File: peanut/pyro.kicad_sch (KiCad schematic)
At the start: 20 parts, among them J1 PYRO_1, J2 PYRO_1, Q1 NMOS, Q2 NMOS, Q3 NMOS, Q4 NMOS

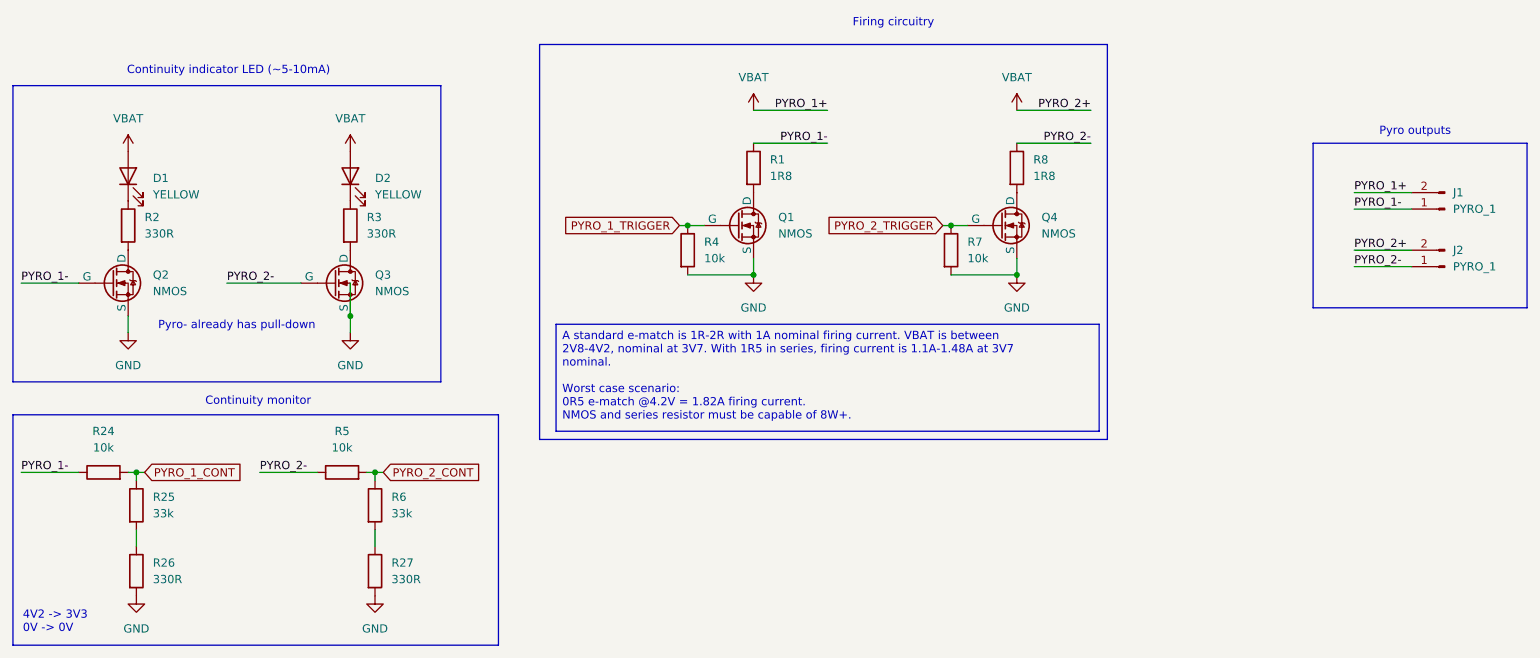
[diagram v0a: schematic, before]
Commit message: Assigned some actual parts and footprints to symbols.
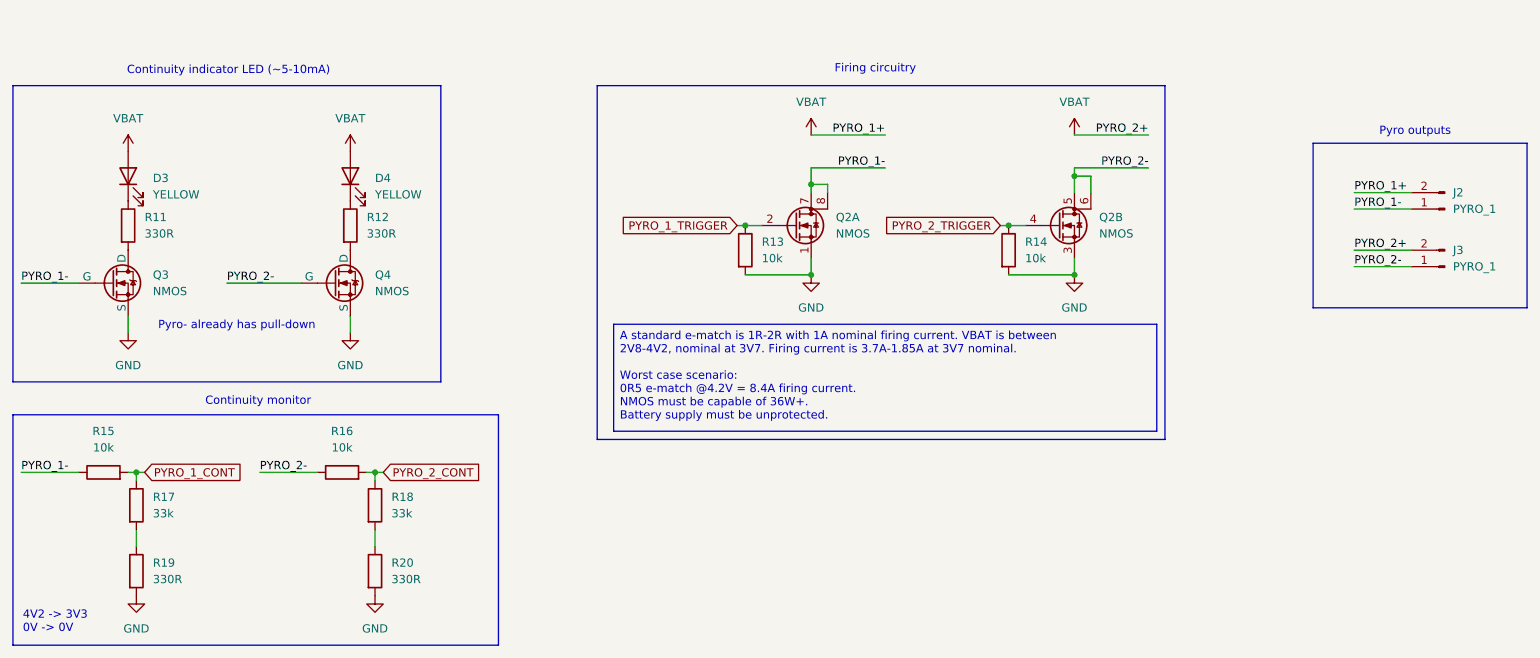
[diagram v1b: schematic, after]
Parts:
- removed Q1, Q4: NMOS, symbol Simulation_SPICE:NMOS
- removed R1, R8: 1R8, symbol Device:R
- added Q2: NMOS, symbol Transistor_FET:Q_Dual_NMOS_S1G1S2G2D2D2D1D1
- D3: renamed from D1; footprint (none) -> LED_SMD:LED_0402_1005Metric
- D4: renamed from D2; footprint (none) -> LED_SMD:LED_0402_1005Metric
- J3: renamed from J2; footprint (none) -> Connector_USB:USB_C_Receptacle_GCT_USB4105-xx-A_16P_TopMnt_Horizontal
- R11: renamed from R2; footprint (none) -> Resistor_SMD:R_0402_1005Metric
- R12: renamed from R3; footprint (none) -> Resistor_SMD:R_0402_1005Metric
- R13: renamed from R4; footprint (none) -> Resistor_SMD:R_0402_1005Metric
- R14: renamed from R7; footprint (none) -> Resistor_SMD:R_0402_1005Metric
- R15: renamed from R24; footprint (none) -> Resistor_SMD:R_0402_1005Metric
- R16: renamed from R5; footprint (none) -> Resistor_SMD:R_0402_1005Metric
- R17: renamed from R25; footprint (none) -> Resistor_SMD:R_0402_1005Metric
- R18: renamed from R6; footprint (none) -> Resistor_SMD:R_0402_1005Metric
- R19: renamed from R26; footprint (none) -> Resistor_SMD:R_0402_1005Metric
- R20: renamed from R27; footprint (none) -> Resistor_SMD:R_0402_1005Metric
- renumbered J1 to J2, Q2 to Q3, Q3 to Q4
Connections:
- net GND: now also Q2.1 (S), Q2.3 (S)
- net PYRO_1-: now also Q2.7 (D), Q2.8 (D)
- net PYRO_1_TRIGGER: now also Q2.2 (G)
- net PYRO_2-: now also Q2.5 (D), Q2.6 (D)
- net PYRO_2_TRIGGER: now also Q2.4 (G)
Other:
- moved on the sheet: R13, R14

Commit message: Footprint assignments for dual-channel NMOS; picked some more parts
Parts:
- D3, D4: MPN (none) -> 599-1140-147F
- Q2: footprint (none) -> TSM200N03DPQ33_RGG:TSM200N03DPQ33RGG
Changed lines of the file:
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@@
 			)
 		)
-		(property "Footprint" ""
+		(property "Footprint" "TSM200N03DPQ33_RGG:TSM200N03DPQ33RGG"
 			(at 199.39 104.14 0)
 			(effects
@@
 			)
 		)
-		(property "Datasheet" "https://www.taiwansemi.com/assets/datasheet/pdf.php?pn=TSM200N03DPQ33"
+		(property "Datasheet" "~"
 			(at 199.39 104.14 0)
 			(effects
@@
 			)
 		)
-		(property "MPN" ""
+		(property "MPN" " 599-1140-147F"
 			(at 85.09 96.52 90)
 			(effects
@@
 			)
 		)
-		(property "MPN" ""
+		(property "MPN" " 599-1140-147F"
 			(at 50.8 96.52 90)
 			(effects
@@
 			)
 		)
-		(property "Footprint" ""
+		(property "Footprint" "TSM200N03DPQ33_RGG:TSM200N03DPQ33RGG"
 			(at 158.75 104.14 0)
 			(effects

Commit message: More component MPNs
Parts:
- D3, D4: MPN 599-1140-147F -> 599-1140-147F
- J3: footprint Connector_USB:USB_C_Receptacle_GCT_USB4105-xx-A_16P_TopMnt_Horizontal -> (none)
- R11, R12, R19, R20: MPN (none) -> 560112110231
- R13, R14, R15, R16: MPN (none) -> SFR01MZPJ103
- R17, R18: MPN (none) -> MR04X3302FTL
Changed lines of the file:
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@@
 			)
 		)
-		(property "MPN" ""
+		(property "MPN" "SFR01MZPJ103"
 			(at 186.69 107.95 0)
 			(effects
@@
 			)
 		)
-		(property "Footprint" "Connector_USB:USB_C_Receptacle_GCT_USB4105-xx-A_16P_TopMnt_Horizontal"
+		(property "Footprint" ""
 			(at 254 110.49 0)
 			(effects
@@
 			)
 		)
-		(property "MPN" ""
+		(property "MPN" "MR04X3302FTL"
 			(at 88.9 147.32 0)
 			(effects
@@
 			)
 		)
-		(property "MPN" " 599-1140-147F"
+		(property "MPN" "599-1140-147F"
 			(at 85.09 96.52 90)
 			(effects
@@
 			)
 		)
-		(property "MPN" ""
+		(property "MPN" "560112110231"
 			(at 85.09 104.14 0)
 			(effects
@@
 			)
 		)
-		(property "MPN" ""
+		(property "MPN" "560112110231"
 			(at 88.9 157.48 0)
 			(effects
@@
 			)
 		)
-		(property "MPN" ""
+		(property "MPN" "560112110231"
 			(at 52.07 157.48 0)
 			(effects
@@
 			)
 		)
-		(property "MPN" " 599-1140-147F"
+		(property "MPN" "599-1140-147F"
 			(at 50.8 96.52 90)
 			(effects
@@
 			)
 		)
-		(property "MPN" ""
+		(property "MPN" "SFR01MZPJ103"
 			(at 83.82 142.24 90)
 			(effects
@@
 			)
 		)
-		(property "MPN" ""
+		(property "MPN" "SFR01MZPJ103"
 			(at 146.05 107.95 0)
 			(effects
@@
 			)
 		)
-		(property "MPN" ""
+		(property "MPN" "SFR01MZPJ103"
 			(at 46.99 142.24 90)
 			(effects
@@
 			)
 		)
-		(property "MPN" ""
+		(property "MPN" "MR04X3302FTL"
 			(at 52.07 147.32 0)
 			(effects
@@
 			)
 		)
-		(property "MPN" ""
+		(property "MPN" "560112110231"
 			(at 50.8 104.14 0)
 			(effects

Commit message: feat: Finish schematic
This commit "completes" the schematic to the best of my foresight for
the moment. All components have BOM MPNs and footprints assigned. I have
double checked pins on the 40MHz clock and that pin assignments on the
MCU are valid. I have selected a chip antenna with high gain, added
decoupling capacitors to the MCU, picked out terminal blocks and
followed the Espressif schematic guide. A preliminary layout can be
made.
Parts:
- removed J2, J3: PYRO_1, symbol Connector:Conn_01x02_Pin
- added J2: PYRO_OUT, TerminalBlock_Phoenix:TerminalBlock_Phoenix_MKDS-1-4-3.81_1x04_P3.81mm_Horizontal, symbol Connector_Generic:Conn_01x04
- Q2: renamed from Q3; footprint (none) -> Package_TO_SOT_SMD:SOT-23-3; MPN (none) -> BSS123NH6327XTSA1
- Q3: renamed from Q4; footprint (none) -> Package_TO_SOT_SMD:SOT-23-3; MPN (none) -> BSS123NH6327XTSA1
- renumbered Q2 to Q4, R15 to R11, R11 to R12, R17 to R13, R19 to R14, R16 to R15, R12 to R16, R18 to R17, R20 to R18, R13 to R19, R14 to R20
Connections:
- net PYRO_1-: now also J2.2 (Pin_2)
- net PYRO_2-: now also J2.4 (Pin_4)
- net VBAT: now also J2.1 (Pin_1), J2.3 (Pin_3)

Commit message: feat: Initial layout
I have roughed out the initial PCB layout. It is wider than I'd like,
and not near a peanut shape. It appears the "start" and "panic" LEDs
never had pins assigned to them. I think I will replace the MCU RX & TX
with these instead, since I can still use the RX and TX as probe pads
that way.
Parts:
- D3, D4: footprint LED_SMD:LED_0402_1005Metric -> LED_SMD:LED_0805_2012Metric
- Q2, Q3: symbol Simulation_SPICE:NMOS -> Transistor_FET_Other:Q_NMOS_Depletion_GSD
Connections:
- net GND: now also Q2.2 (S), Q3.2 (S); no longer Q2.3 (S), Q3.3 (S)
- net PYRO_1-: now also J2.4 (Pin_4), Q2.1 (G); no longer J2.2 (Pin_2), Q2.2 (G)
- net PYRO_2-: now also J2.2 (Pin_2), Q3.1 (G); no longer J2.4 (Pin_4), Q3.2 (G)
- net at R16.2: now also Q3.3 (D); no longer Q3.1 (D)
- net at R12.2: now also Q2.3 (D); no longer Q2.1 (D)
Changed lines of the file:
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@@
 	)
 	(label "PYRO_2-"
-		(at 237.49 104.14 0)
+		(at 237.49 99.06 0)
 		(effects
 			(font
@@
 		)
 	)
-	(label "PYRO_2+"
-		(at 237.49 101.6 0)
-		(effects
-			(font
-				(size 1.27 1.27)
-			)
-			(justify left bottom)
-		)
-	)
-	(label "PYRO_1+"
-		(at 237.49 96.52 0)
+	(label "PYRO_1-"
+		(at 237.49 104.14 0)
 		(effects
 			(font
@@
 		)
 	)
+	(label "PYRO_1+"
+		(at 237.49 101.6 0)
+		(effects
+			(font
+				(size 1.27 1.27)
+			)
+			(justify left bottom)
+		)
+	)
 	(label "PYRO_1-"
 		(at 34.29 142.24 0)
@@
 		)
 	)
-	(label "PYRO_1-"
-		(at 237.49 99.06 0)
+	(label "PYRO_2+"
+		(at 237.49 96.52 0)
 		(effects
 			(font
@@
 			)
 		)
-		(property "Footprint" "LED_SMD:LED_0402_1005Metric"
+		(property "Footprint" "LED_SMD:LED_0805_2012Metric"
 			(at 85.09 96.52 0)
 			(hide yes)
@@
 	)
 	(symbol
-		(lib_id "Simulation_SPICE:NMOS")
+		(lib_id "Transistor_FET_Other:Q_NMOS_Depletion_GSD")
 		(at 48.26 113.03 0)
 		(unit 1)
@@
 		)
 		(property "Footprint" "Package_TO_SOT_SMD:SOT-23-3"
-			(at 53.34 110.49 0)
+			(at 48.26 113.03 0)
 			(hide yes)
 			(show_name no)
@@
 		)
 		(property "Datasheet" "https://www.mouser.ca/datasheet/3/70/1/Infineon_BSS123N_DataSheet_v02_03_en.pdf"
-			(at 48.26 125.73 0)
-			(hide yes)
-			(show_name no)
-			(do_not_autoplace no)
-			(effects
-				(font
-					(size 1.27 1.27)
-				)
-			)
-		)
-		(property "Description" "N-MOSFET transistor, drain/source/gate"
+			(at 48.26 113.03 0)
+			(hide yes)
+			(show_name no)
+			(do_not_autoplace no)
+			(effects
+				(font
+					(size 1.27 1.27)
+				)
+			)
+		)
+		(property "Description" "Depletion-mode N-channel MOSFET gate/source/drain"
 			(at 48.26 113.03 0)
 			(hide yes)
@@
 			)
 		)
-		(property "Footprint" "LED_SMD:LED_0402_1005Metric"
+		(property "Footprint" "LED_SMD:LED_0805_2012Metric"
 			(at 50.8 96.52 0)
 			(hide yes)
@@
 	)
 	(symbol
-		(lib_id "Simulation_SPICE:NMOS")
+		(lib_id "Transistor_FET_Other:Q_NMOS_Depletion_GSD")
 		(at 82.55 113.03 0)
 		(unit 1)
@@
 		)
 		(property "Footprint" "Package_TO_SOT_SMD:SOT-23-3"
-			(at 87.63 110.49 0)
+			(at 82.55 113.03 0)
 			(hide yes)
 			(show_name no)
@@
 		)
 		(property "Datasheet" "https://www.mouser.ca/datasheet/3/70/1/Infineon_BSS123N_DataSheet_v02_03_en.pdf"
-			(at 82.55 125.73 0)
-			(hide yes)
-			(show_name no)
-			(do_not_autoplace no)
-			(effects
-				(font
-					(size 1.27 1.27)
-				)
-			)
-		)
-		(property "Description" "N-MOSFET transistor, drain/source/gate"
 			(at 82.55 113.03 0)
 			(hide yes)
+			(show_name no)
+			(do_not_autoplace no)
+			(effects
+				(font
+					(size 1.27 1.27)
+				)
+			)
+		)
+		(property "Description" "Depletion-mode N-channel MOSFET gate/source/drain"
+			(at 82.55 113.03 0)
+			(hide yes)

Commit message: feat: Better layout
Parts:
- renumbered D3 to D2, D4 to D3, R11 to R10, R12 to R11, R13 to R12, R14 to R13, R15 to R14, R16 to R15, R17 to R16, R18 to R17, R19 to R18, R20 to R19
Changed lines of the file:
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@@
 		(dnp no)
 		(fields_autoplaced yes)
-		(property "Reference" "#PWR040"
+		(property "Reference" "#PWR038"
 			(at 196.85 118.11 0)
 			(hide yes)
@@
 			(project "peanut"
 				(path "/5c6b6cfc-6c84-425a-9b66-e6111713aae8/4be069cc-6620-4cc3-a173-eaa174b1ef03"
-					(reference "#PWR040")
+					(reference "#PWR038")
 					(unit 1)
 				)
@@
 		(dnp no)
 		(fields_autoplaced yes)
-		(property "Reference" "R20"
+		(property "Reference" "R19"
 			(at 189.23 106.6799 0)
 			(show_name no)
@@
 			(project "peanut"
 				(path "/5c6b6cfc-6c84-425a-9b66-e6111713aae8/4be069cc-6620-4cc3-a173-eaa174b1ef03"
-					(reference "R20")
+					(reference "R19")
 					(unit 1)
 				)
@@
 		(dnp no)
 		(fields_autoplaced yes)
-		(property "Reference" "#PWR039"
+		(property "Reference" "#PWR037"
 			(at 196.85 93.98 0)
 			(hide yes)
@@
 			(project "peanut"
 				(path "/5c6b6cfc-6c84-425a-9b66-e6111713aae8/4be069cc-6620-4cc3-a173-eaa174b1ef03"
-					(reference "#PWR039")
+					(reference "#PWR037")
 					(unit 1)
 				)
@@
 		(dnp no)
 		(fields_autoplaced yes)
-		(property "Reference" "R17"
+		(property "Reference" "R16"
 			(at 91.44 146.0499 0)
 			(show_name no)
@@
 			(project "peanut"
 				(path "/5c6b6cfc-6c84-425a-9b66-e6111713aae8/4be069cc-6620-4cc3-a173-eaa174b1ef03"
-					(reference "R17")
+					(reference "R16")
 					(unit 1)
 				)
@@
 		(dnp no)
 		(fields_autoplaced yes)
-		(property "Reference" "D4"
+		(property "Reference" "D3"
 			(at 88.9 96.8374 90)
 			(show_name no)
@@
 			(project "peanut"
 				(path "/5c6b6cfc-6c84-425a-9b66-e6111713aae8/4be069cc-6620-4cc3-a173-eaa174b1ef03"
-					(reference "D4")
+					(reference "D3")
 					(unit 1)
 				)
@@
 		(dnp no)
 		(fields_autoplaced yes)
-		(property "Reference" "#PWR038"
+		(property "Reference" "#PWR036"
 			(at 156.21 118.11 0)
 			(hide yes)
@@
 			(project "peanut"
 				(path "/5c6b6cfc-6c84-425a-9b66-e6111713aae8/4be069cc-6620-4cc3-a173-eaa174b1ef03"
-					(reference "#PWR038")
+					(reference "#PWR036")
 					(unit 1)
 				)
@@
 		(dnp no)
 		(fields_autoplaced yes)
-		(property "Reference" "R16"
+		(property "Reference" "R15"
 			(at 87.63 102.8699 0)
 			(show_name no)
@@
 			(project "peanut"
 				(path "/5c6b6cfc-6c84-425a-9b66-e6111713aae8/4be069cc-6620-4cc3-a173-eaa174b1ef03"
-					(reference "R16")
+					(reference "R15")
 					(unit 1)
 				)
@@
 		(dnp no)
 		(fields_autoplaced yes)
-		(property "Reference" "#PWR032"
+		(property "Reference" "#PWR030"
 			(at 50.8 127 0)
 			(hide yes)
@@
 			(project "peanut"
 				(path "/5c6b6cfc-6c84-425a-9b66-e6111713aae8/4be069cc-6620-4cc3-a173-eaa174b1ef03"
-					(reference "#PWR032")
+					(reference "#PWR030")
 					(unit 1)
 				)
@@
 		(dnp no)
 		(fields_autoplaced yes)
-		(property "Reference" "R18"
+		(property "Reference" "R17"
 			(at 91.44 156.2099 0)
 			(show_name no)
@@
 			(project "peanut"
 				(path "/5c6b6cfc-6c84-425a-9b66-e6111713aae8/4be069cc-6620-4cc3-a173-eaa174b1ef03"
-					(reference "R18")
+					(reference "R17")
 					(unit 1)
 				)
@@
 		(dnp no)
 		(fields_autoplaced yes)
-		(property "Reference" "R14"
+		(property "Reference" "R13"
 			(at 54.61 156.2099 0)
 			(show_name no)
@@
 			(project "peanut"
 				(path "/5c6b6cfc-6c84-425a-9b66-e6111713aae8/4be069cc-6620-4cc3-a173-eaa174b1ef03"
-					(reference "R14")
+					(reference "R13")
 					(unit 1)
 				)
@@
 		(dnp no)
 		(fields_autoplaced yes)
-		(property "Reference" "#PWR035"
+		(property "Reference" "#PWR033"
 			(at 85.09 127 0)
 			(hide yes)
@@
 			(project "peanut"
 				(path "/5c6b6cfc-6c84-425a-9b66-e6111713aae8/4be069cc-6620-4cc3-a173-eaa174b1ef03"
-					(reference "#PWR035")
+					(reference "#PWR033")
 					(unit 1)
 				)
@@
 		(dnp no)
 		(fields_autoplaced yes)
-		(property "Reference" "#PWR036"
+		(property "Reference" "#PWR034"
 			(at 88.9 167.64 0)
 			(hide yes)
@@
 			(project "peanut"
 				(path "/5c6b6cfc-6c84-425a-9b66-e6111713aae8/4be069cc-6620-4cc3-a173-eaa174b1ef03"
-					(reference "#PWR036")
+					(reference "#PWR034")
 					(unit 1)
 				)
@@
 		(dnp no)
 		(fields_autoplaced yes)
-		(property "Reference" "D3"
+		(property "Reference" "D2"
 			(at 54.61 96.8374 90)
 			(show_name no)
@@
 			(project "peanut"
 				(path "/5c6b6cfc-6c84-425a-9b66-e6111713aae8/4be069cc-6620-4cc3-a173-eaa174b1ef03"
-					(reference "D3")
+					(reference "D2")
 					(unit 1)
 				)
@@
 		(dnp no)
 		(fields_autoplaced yes)
-		(property "Reference" "#PWR033"
+		(property "Reference" "#PWR031"
 			(at 52.07 167.64 0)
 			(hide yes)
@@
 			(project "peanut"
 				(path "/5c6b6cfc-6c84-425a-9b66-e6111713aae8/4be069cc-6620-4cc3-a173-eaa174b1ef03"
-					(reference "#PWR033")
+					(reference "#PWR031")
 					(unit 1)
 				)
@@
 		(dnp no)
 		(fields_autoplaced yes)
-		(property "Reference" "R15"
+		(property "Reference" "R14"
 			(at 83.82 135.89 90)
 			(show_name no)
@@
 			(project "peanut"
 				(path "/5c6b6cfc-6c84-425a-9b66-e6111713aae8/4be069cc-6620-4cc3-a173-eaa174b1ef03"
-					(reference "R15")
+					(reference "R14")
 					(unit 1)
 				)
@@
 		(dnp no)
 		(fields_autoplaced yes)
-		(property "Reference" "R19"
+		(property "Reference" "R18"
 			(at 148.59 106.6799 0)
 			(show_name no)
@@
 			(project "peanut"
 				(path "/5c6b6cfc-6c84-425a-9b66-e6111713aae8/4be069cc-6620-4cc3-a173-eaa174b1ef03"
-					(reference "R19")
+					(reference "R18")
 					(unit 1)
 				)
@@
 		(dnp no)
 		(fields_autoplaced yes)
-		(property "Reference" "#PWR037"
+		(property "Reference" "#PWR035"
 			(at 156.21 93.98 0)
 			(hide yes)
@@
 			(project "peanut"
 				(path "/5c6b6cfc-6c84-425a-9b66-e6111713aae8/4be069cc-6620-4cc3-a173-eaa174b1ef03"
-					(reference "#PWR037")
+					(reference "#PWR035")
 					(unit 1)
 				)
@@
 		(dnp no)
 		(fields_autoplaced yes)
-		(property "Reference" "#PWR031"
+		(property "Reference" "#PWR029"
 			(at 50.8 96.52 0)
 			(hide yes)
@@
 			(project "peanut"
 				(path "/5c6b6cfc-6c84-425a-9b66-e6111713aae8/4be069cc-6620-4cc3-a173-eaa174b1ef03"
-					(reference "#PWR031")
+					(reference "#PWR029")
 					(unit 1)
 				)
@@
 		(dnp no)
 		(fields_autoplaced yes)
-		(property "Reference" "#PWR034"
+		(property "Reference" "#PWR032"
 			(at 85.09 96.52 0)
 			(hide yes)
@@
 			(project "peanut"
 				(path "/5c6b6cfc-6c84-425a-9b66-e6111713aae8/4be069cc-6620-4cc3-a173-eaa174b1ef03"
-					(reference "#PWR034")
+					(reference "#PWR032")
 					(unit 1)
 				)
@@
 		(dnp no)
 		(fields_autoplaced yes)
-		(property "Reference" "R11"
+		(property "Reference" "R10"
 			(at 46.99 135.89 90)
 			(show_name no)
@@
 			(project "peanut"
 				(path "/5c6b6cfc-6c84-425a-9b66-e6111713aae8/4be069cc-6620-4cc3-a173-eaa174b1ef03"
-					(reference "R11")
+					(reference "R10")
 					(unit 1)
 				)
@@
 		(dnp no)
 		(fields_autoplaced yes)
-		(property "Reference" "R13"
+		(property "Reference" "R12"
 			(at 54.61 146.0499 0)
 			(show_name no)
@@
 			(project "peanut"
 				(path "/5c6b6cfc-6c84-425a-9b66-e6111713aae8/4be069cc-6620-4cc3-a173-eaa174b1ef03"
-					(reference "R13")
+					(reference "R12")
 					(unit 1)
 				)
@@
 		(dnp no)
 		(fields_autoplaced yes)
-		(property "Reference" "R12"
+		(property "Reference" "R11"
 			(at 53.34 102.8699 0)
 			(show_name no)
@@
 			(project "peanut"
 				(path "/5c6b6cfc-6c84-425a-9b66-e6111713aae8/4be069cc-6620-4cc3-a173-eaa174b1ef03"
-					(reference "R12")
-					(unit 1)
-				)
+					(reference "R11")
+					(unit 1)
+				)
